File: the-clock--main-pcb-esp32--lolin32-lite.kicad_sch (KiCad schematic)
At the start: 17 parts, among them J1 Conn_01x04, SW1 SW_Push, SW2 SW_Push, SW3 SW_Push, SW4 SW_Push

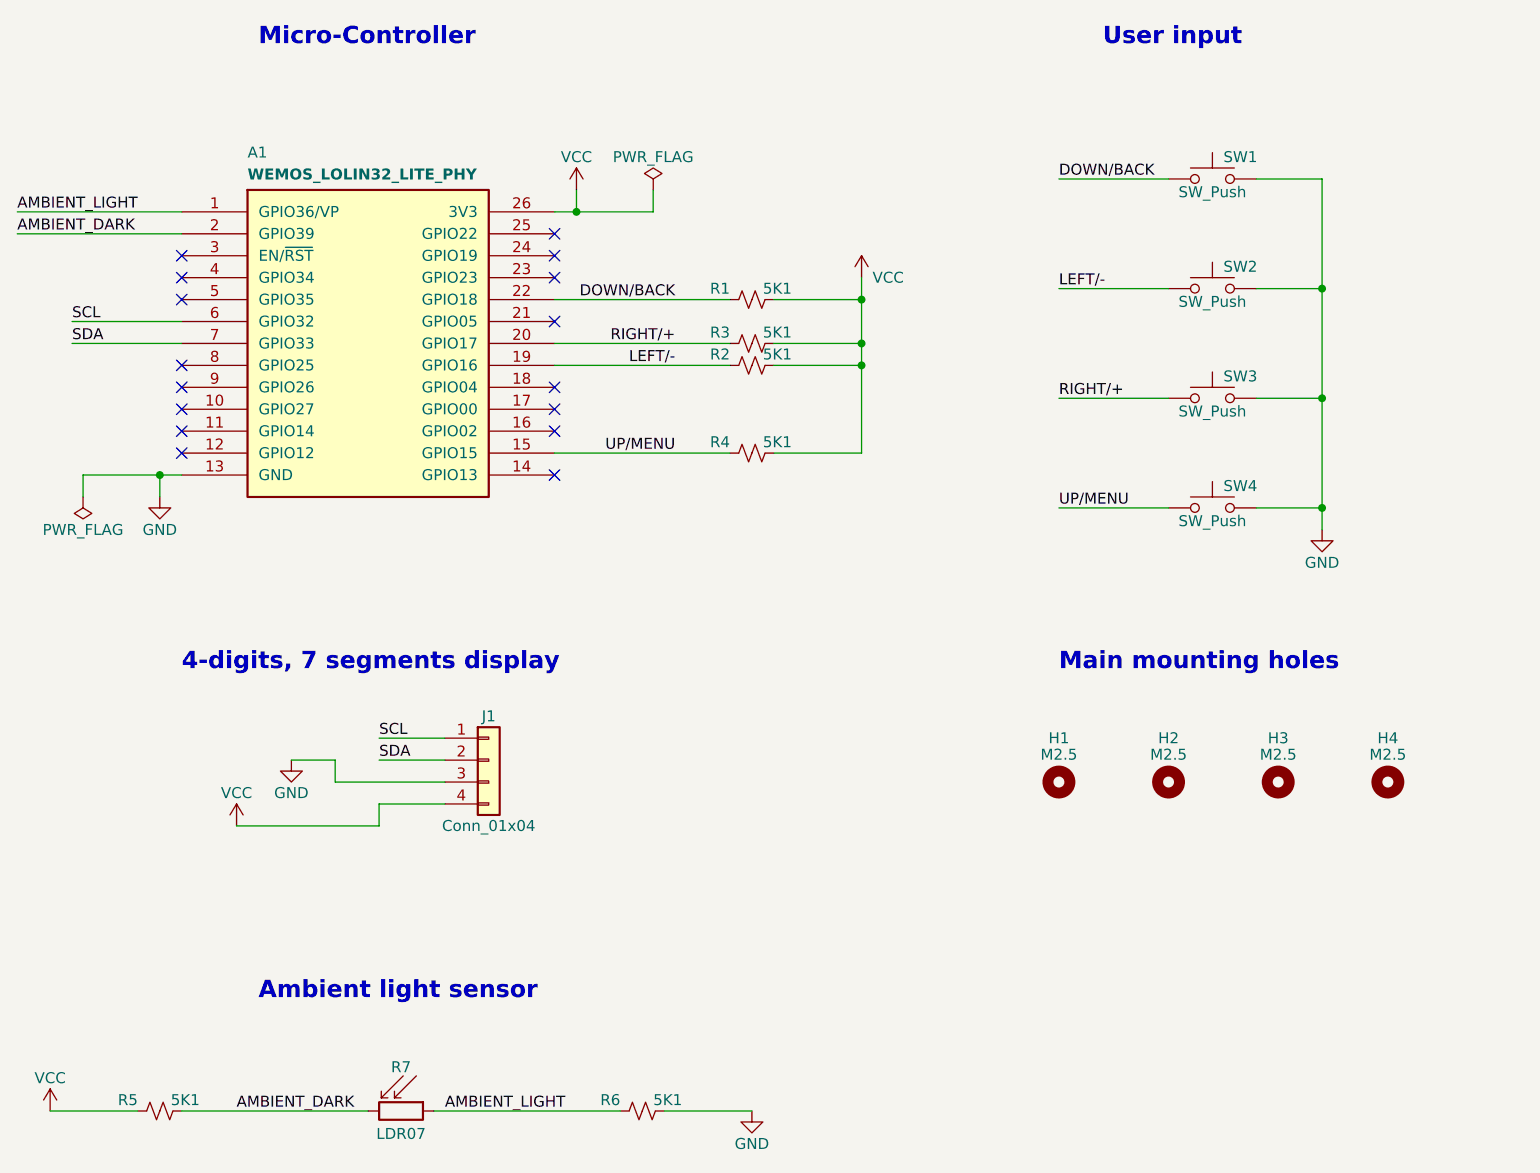
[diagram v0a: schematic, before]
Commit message: Fixed : missing pull-up resistors for SDA/SCL
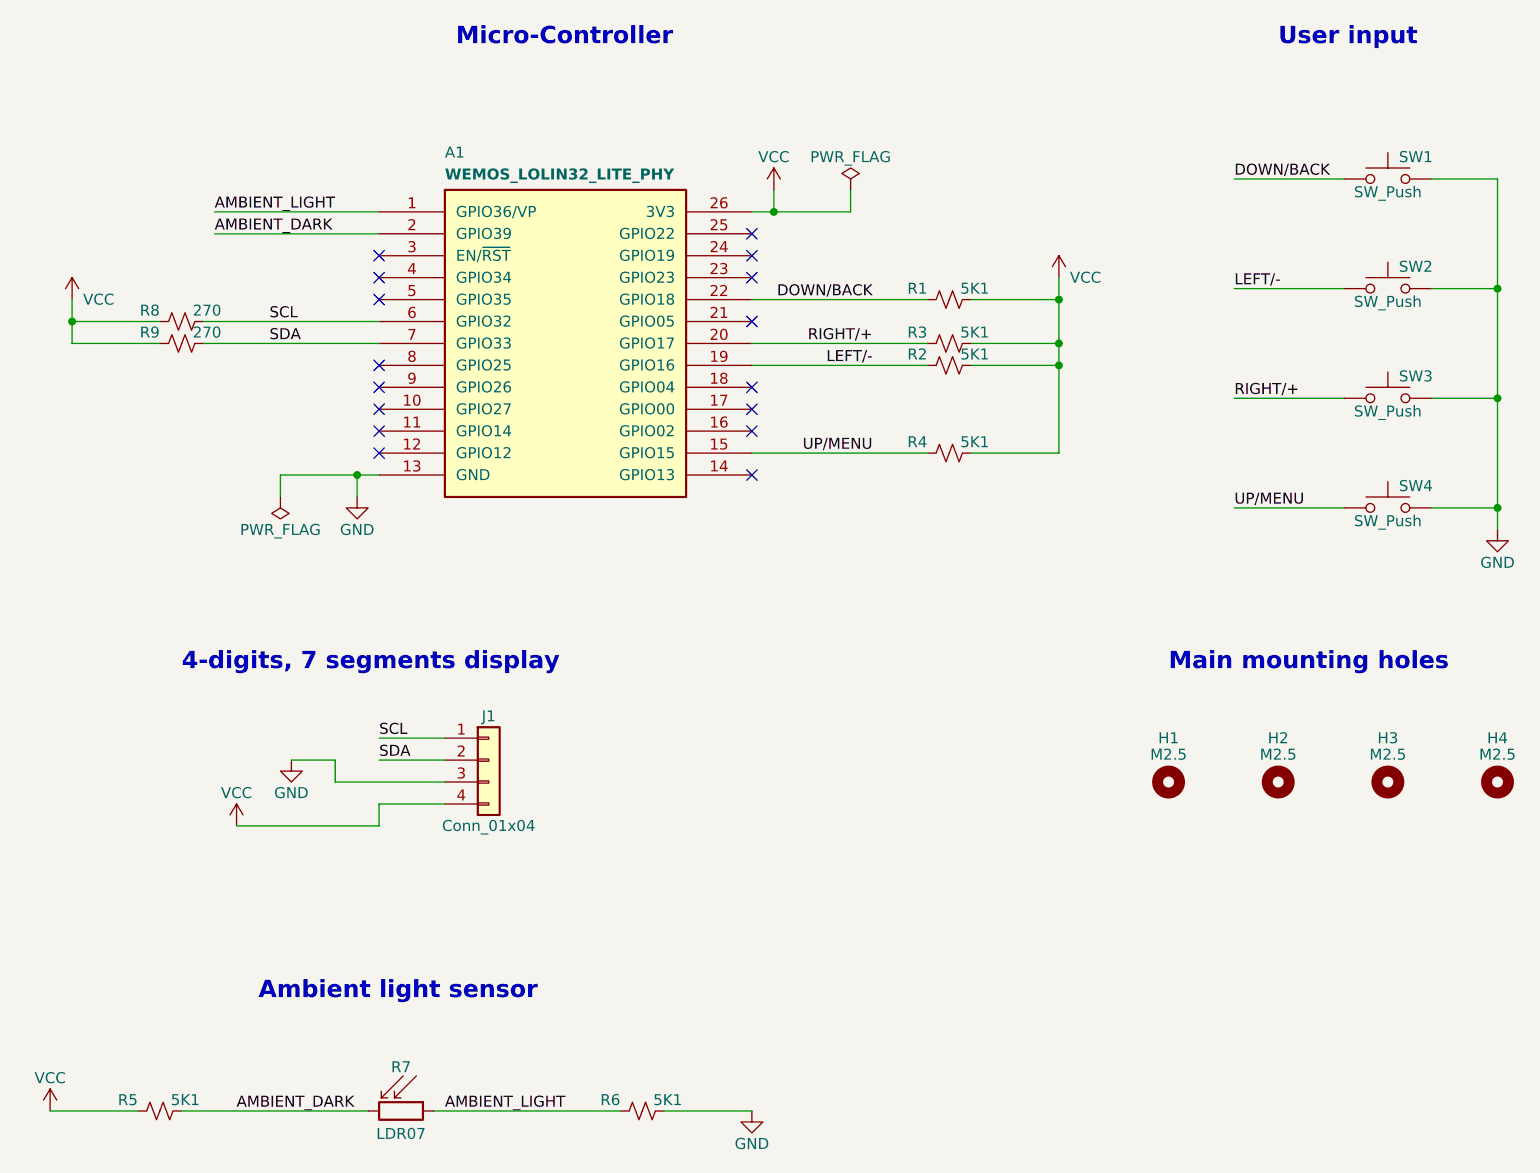
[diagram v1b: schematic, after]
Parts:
- added R8, R9: 270, commons-passives_THT:Passive_THT_resistor_W2.54mm_L10.16mm, symbol Device:R_Small_US
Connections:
- net SCL: now also R8.2
- net SDA: now also R9.2
- net VCC: now also R8.1, R9.1
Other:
- moved on the sheet: A1, H1, H2, H3, H4, R1, R2, R3, R4, SW1, SW2, SW3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
